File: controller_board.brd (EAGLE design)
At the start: 144 x 118 mm, 48 parts, among them J1 FRSKY-GIMBAL, J12 JST_3PIN_GND_VDD_SIG, J14 JST_3PIN_GND_VDD_SIG, J16 JST_3PIN_GND_VDD_SIG, J18 JST_3PIN_GND_VDD_SIG, J2 FRSKY-GIMBAL, J3 WIRE-HARNESS-SPARKFUN-9915, J6 HEADER-0.1IN-6POS-SCREW, J7 HEADER-0.1IN-6POS-FEMALE

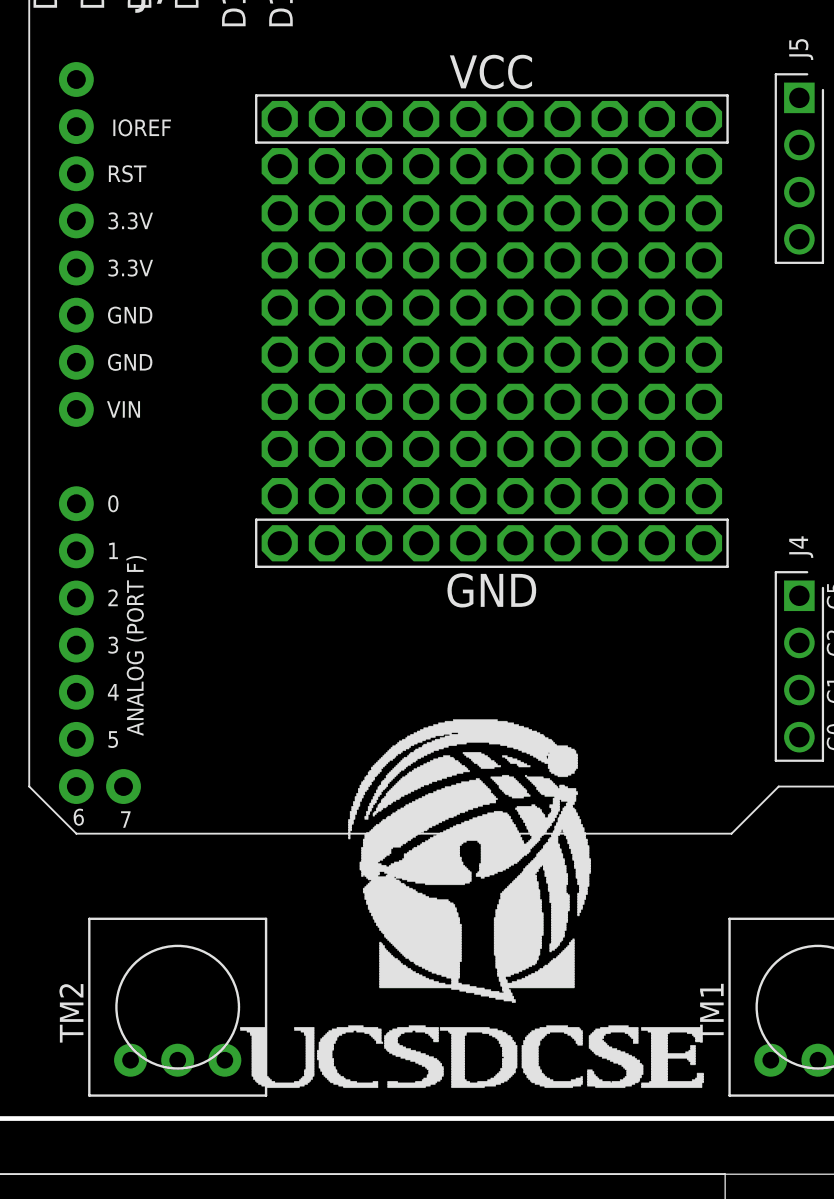
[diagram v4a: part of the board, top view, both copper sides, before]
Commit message: small tweak it logo position
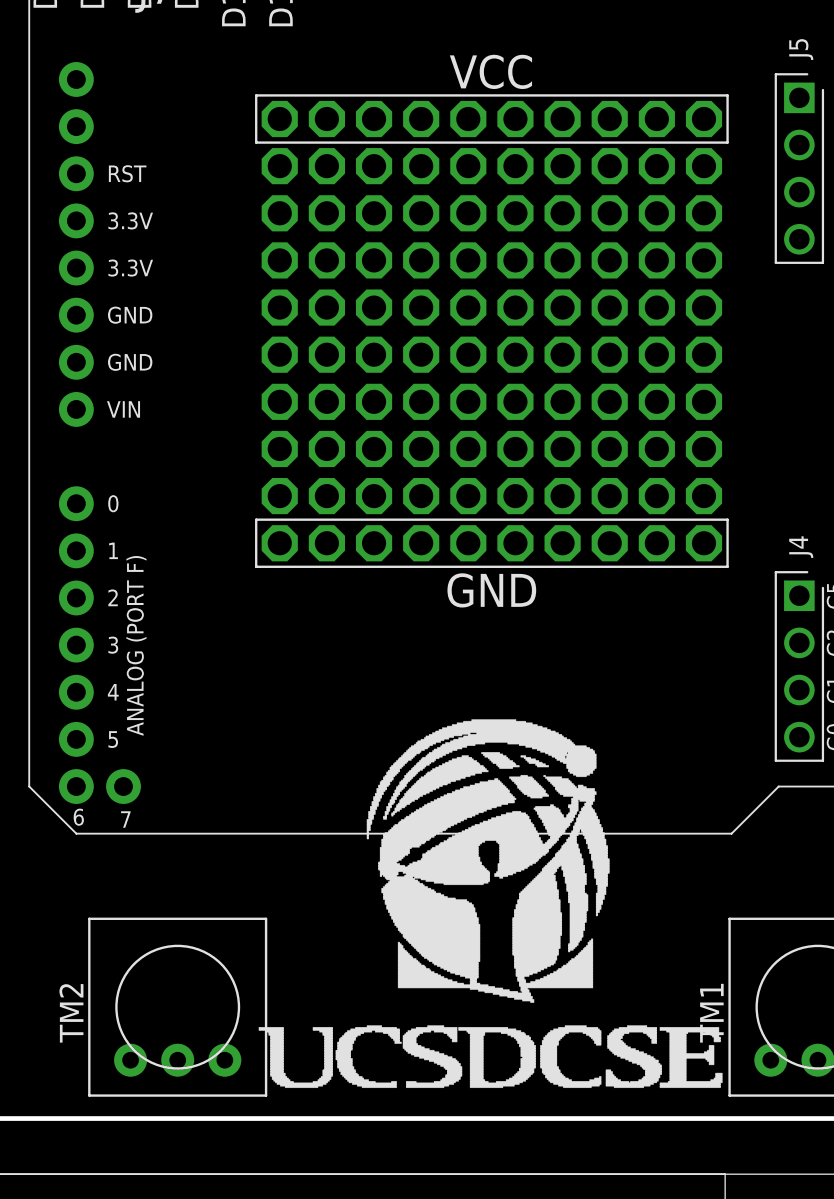
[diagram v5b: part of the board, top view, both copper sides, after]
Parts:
- moved U$1 1.00 mm to (-15.5, 7.50)
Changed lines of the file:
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@@
 <layer number="49" name="Reference" color="7" fill="1" visible="yes" active="yes"/>
 <layer number="50" name="dxf" color="7" fill="1" visible="yes" active="yes"/>
-<layer number="51" name="tDocu" color="7" fill="1" visible="no" active="yes"/>
+<layer number="51" name="tDocu" color="7" fill="1" visible="yes" active="yes"/>
 <layer number="52" name="bDocu" color="7" fill="1" visible="yes" active="yes"/>
 <layer number="53" name="tGND_GNDA" color="7" fill="1" visible="yes" active="yes"/>
@@
 <attribute name="DISTPN" value="1010" x="-54" y="-47" size="1.778" layer="27" display="off"/>
 <attribute name="DIST" value="ADAFRUIT" x="-54" y="-47" size="1.778" layer="27" display="off"/>
+<attribute name="MISC" value="temp" x="-54" y="-47" size="1.778" layer="27" display="off"/>
 </element>
 <element name="OUTLINE" library="RemotePartsA" package="CONTROLLER_OUTLINE" value="" x="0" y="0" locked="yes"/>
@@
 <attribute name="ROUGH_HEIGHT" value="16" x="-53" y="11.5" size="1.778" layer="27" rot="R270" display="off"/>
 </element>
-<element name="U$1" library="Artwork" package="CSE_LOGO_30X20MM" value="" x="-16.5" y="7.5"/>
+<element name="U$1" library="Artwork" package="CSE_LOGO_30X20MM" value="" x="-15.5" y="7.5"/>
 <element name="U$2" library="Artwork" package="UCSD_LOGO_COMBINED_26X20MM" value="" x="11" y="20" rot="MR0"/>
 <element name="RESET" library="Controller" package="BUTTON-TACTILE-SQUARE-ADAFRUIT1010" value="BUTTON-TACTILE-SQUARE" x="-53.5" y="49.5">
 <attribute name="DISTPN" value="1010" x="-53.5" y="49.5" size="1.778" layer="27" display="off"/>
 <attribute name="DIST" value="ADAFRUIT" x="-53.5" y="49.5" size="1.778" layer="27" display="off"/>
+<attribute name="MISC" value="temp" x="-53.5" y="49.5" size="1.778" layer="27" display="off"/>
 </element>
 <element name="J11" library="Components" package="SCREW-TERMINAL-1X3-2.54MM" value="" x="52.5" y="-36" smashed="yes" rot="R90">
@@
 <attribute name="DISTPN" value="1010" x="54" y="-47" size="1.778" layer="27" display="off"/>
 <attribute name="DIST" value="ADAFRUIT" x="54" y="-47" size="1.778" layer="27" display="off"/>
+<attribute name="MISC" value="temp" x="54" y="-47" size="1.778" layer="27" display="off"/>
 </element>
 <element name="GND" library="Components" package="SCREW-TERMINAL-1X3-2.54MM" value="" x="14.5" y="54.5" smashed="yes">
